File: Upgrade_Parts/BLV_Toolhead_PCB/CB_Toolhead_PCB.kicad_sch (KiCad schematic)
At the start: 10 parts, among them J1 Micro-Fit, J2 JST-4, J3 JST-2, J4 JST-2, J5 JST-2, J6 JST-2, J7 Endstop, J8 JST-3, J9 JST-2

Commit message: termination fix
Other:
- note added: "Accelerometer LIS3DH RJ45 Con"
- note removed: "Accelerometer"
- company: (none) -> https://github.com/Battosai42/CraftbotPlus_Upgrade
- title: (none) -> BLF Toolhaed PCB
- moved on the sheet: J1, J2, TH1

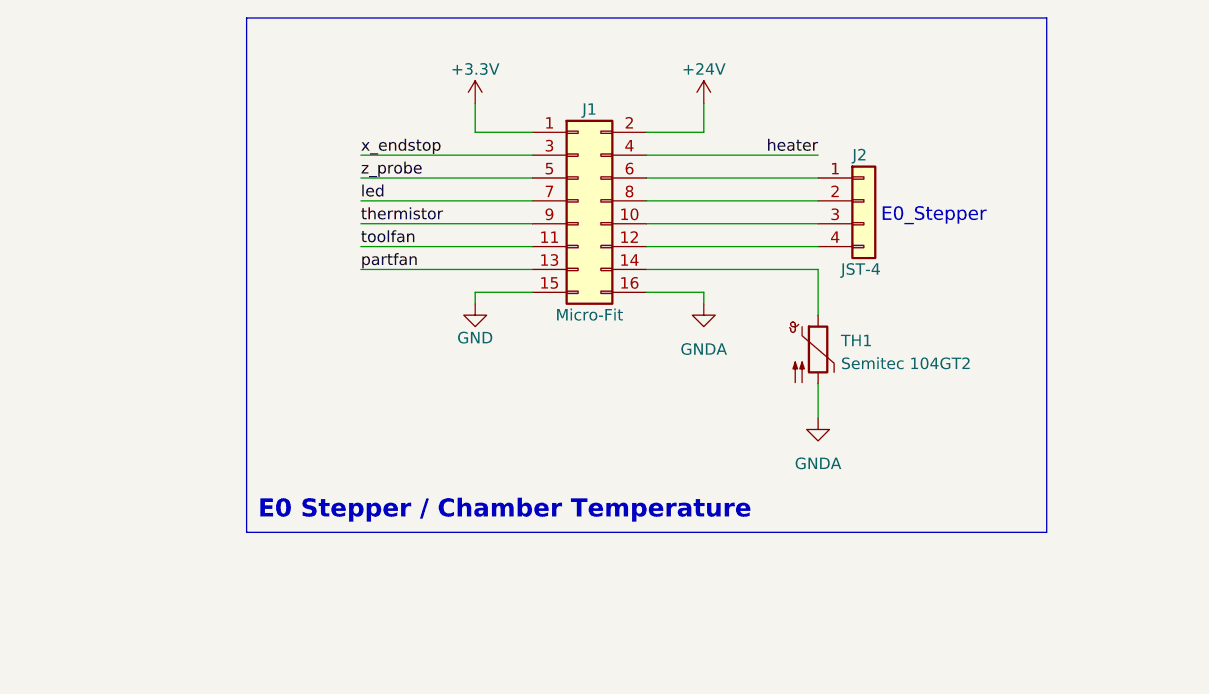
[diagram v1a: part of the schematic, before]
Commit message: using 3.3V LVDS driver
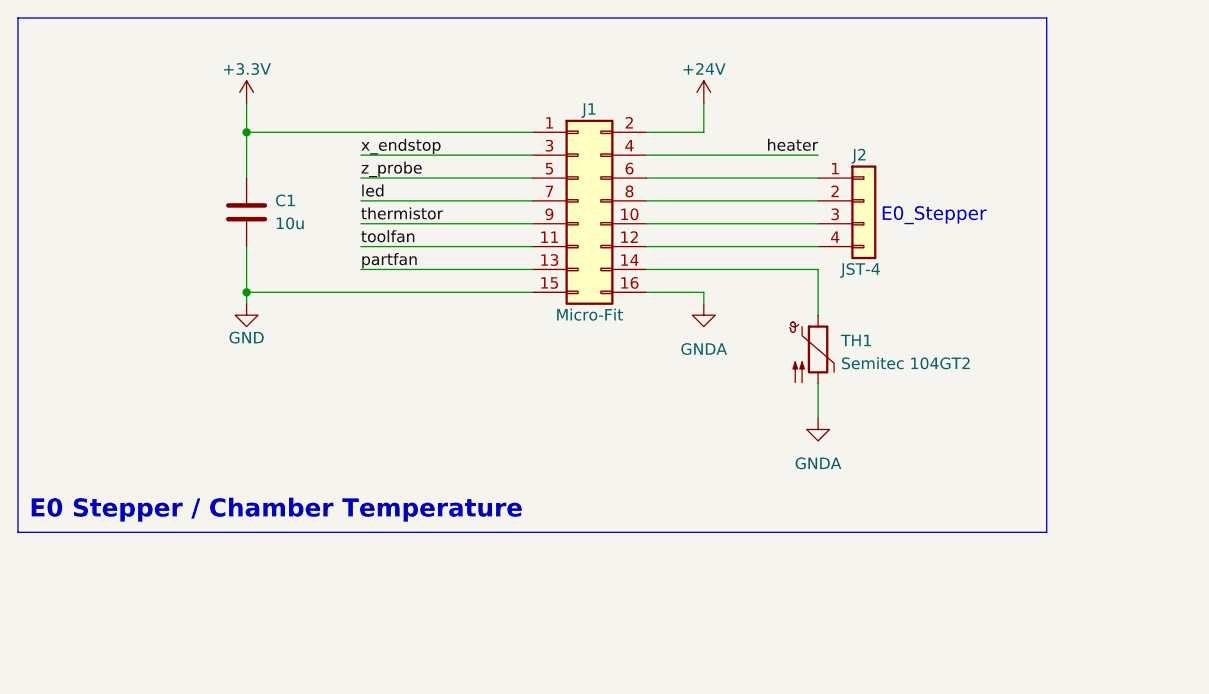
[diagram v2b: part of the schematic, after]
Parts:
- added C1: 10u, symbol Device:C
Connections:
- net +3V3: now also C1.1
- net GND: now also C1.2

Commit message: cleanup
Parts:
- added H1, H2, H3, H4: M3_Mount, symbol Mechanical:MountingHole_Pad
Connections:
- net GND: now also H1.1, H2.1, H3.1, H4.1
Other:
- note added: "Accelerometer"
- note added: "LIS3DH RJ45 Con"
- note removed: "Accelerometer LIS3DH RJ45 Con"
- moved on the sheet: C1, J1, J2, TH1

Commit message: replaced lvds drver
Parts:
- C1: footprint (none) -> Capacitor_SMD:C_0603_1608Metric
- H1, H2, H3, H4: footprint (none) -> MountingHole:MountingHole_3.2mm_M3_DIN965_Pad
- J1: footprint Connector_Molex:Molex_Micro-Fit_3.0_43045-1612_2x08_P3.00mm_Vertical -> Connector_Molex:Molex_Micro-Fit_3.0_43045-1621_2x08-1MP_P3.00mm_Horizontal
- J7: footprint (none) -> Connector_JST:JST_EH_B3B-EH-A_1x03_P2.50mm_Vertical

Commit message: new page for periphery
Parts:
- removed J3, J4, J5, J6, J9: JST-2, Connector_JST:JST_EH_B2B-EH-A_1x02_P2.50mm_Vertical, symbol Connector_Generic:Conn_01x02
- removed J7: Endstop, Connector_JST:JST_EH_B3B-EH-A_1x03_P2.50mm_Vertical, symbol Connector_Generic:Conn_01x03
- removed J8: JST-3, Connector_JST:JST_EH_B3B-EH-A_1x03_P2.50mm_Vertical, symbol Connector_Generic:Conn_01x03
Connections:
- net 1A: now reaches J1.6 (Pin_6), J2.1 (Pin_1)
- net 1B: now reaches J1.8 (Pin_8), J2.2 (Pin_2)
- net 2A: now reaches J1.10 (Pin_10), J2.3 (Pin_3)
- net 2B: now reaches J1.12 (Pin_12), J2.4 (Pin_4)
- no-connect marks 1 -> 0
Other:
- added sheet Periphery (periphery.kicad_sch)
- note added: "Board2Wire Connector"
- note added: "Extruder"
- note removed: "E0 Stepper / Chamber Temperature"
- note removed: "E0_Heater"
- note removed: "E0_Partfan"
- note removed: "E0_Thermistor"
- note removed: "E0_Toolfan"
- note removed: "Hotend / Endstop / Probe"
- note removed: "IR_Probe"
- note removed: "Toolhead LED"
- note removed: "X-Endstop"
- moved on the sheet: C1, J1, J2, TH1

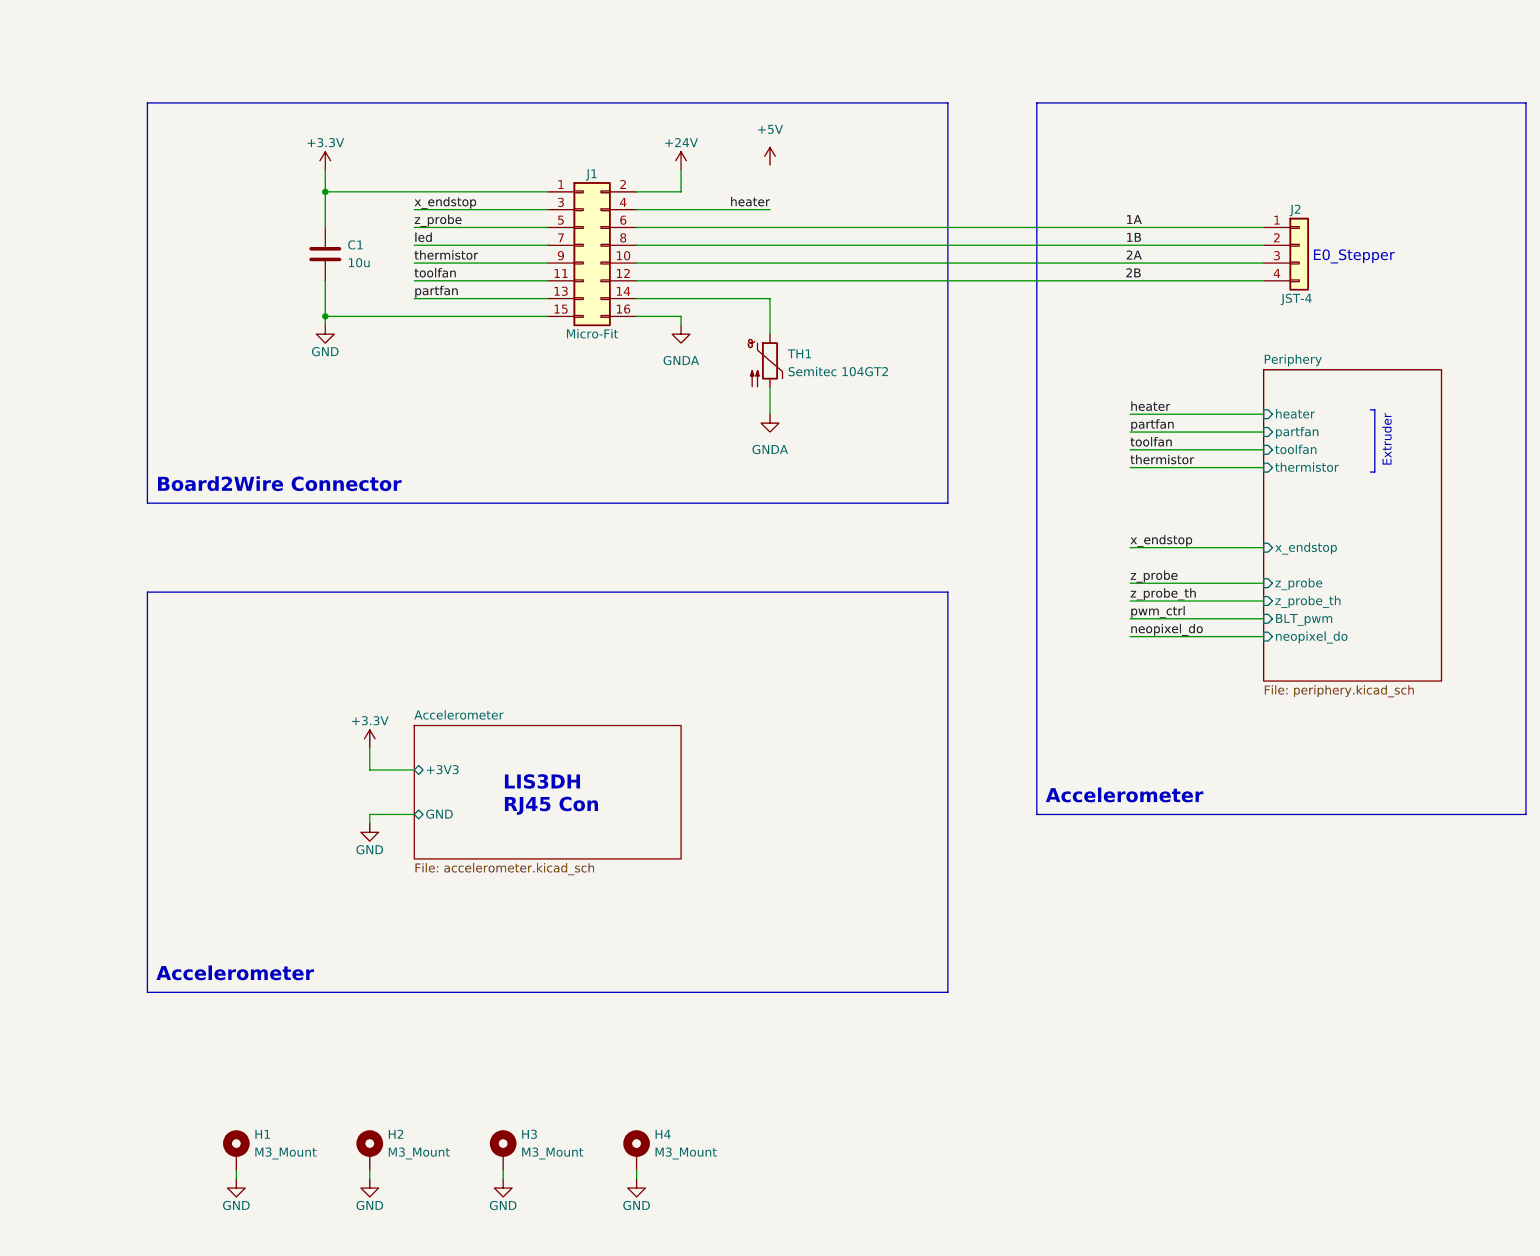
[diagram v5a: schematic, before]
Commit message: removed lvds drivers
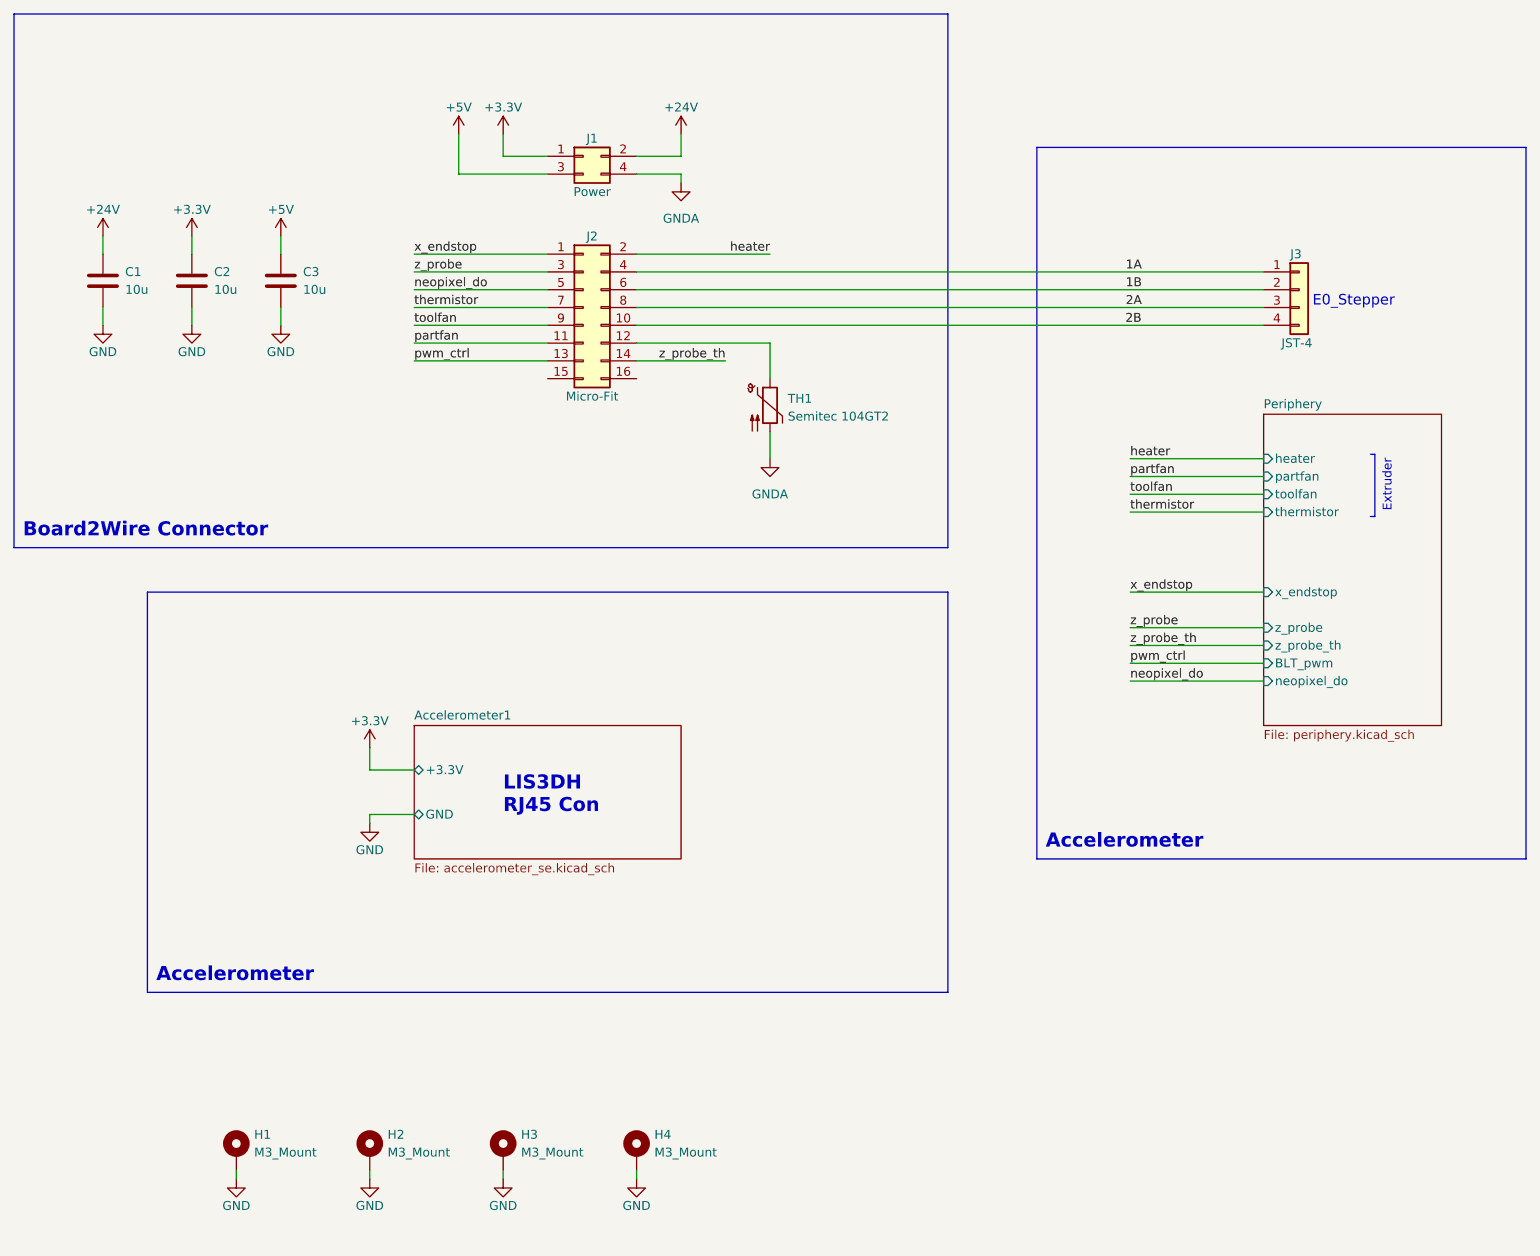
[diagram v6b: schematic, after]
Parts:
- added C1, C2: 10u, Capacitor_SMD:C_0603_1608Metric, symbol Device:C
- added J1: Power, Connector_Molex:Molex_Micro-Fit_3.0_43045-0421_2x02-1MP_P3.00mm_Horizontal, symbol Connector_Generic:Conn_02x02_Odd_Even
- renumbered C1 to C3, J1 to J2, J2 to J3
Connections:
- net led is gone; now on net thermistor: J2.7 (Pin_7)
- net +24V: now also C1.1, J1.2 (Pin_2); no longer J2.2 (Pin_2)
- net +3V3: now also C2.1, J1.1 (Pin_1); no longer C3.1, J2.1 (Pin_1)
- net +5V: now also C3.1, J1.3 (Pin_3)
- net 1A: now also J2.4 (Pin_4); no longer J2.6 (Pin_6)
- net 1B: now also J2.6 (Pin_6); no longer J2.8 (Pin_8)
- net 2A: now also J2.8 (Pin_8); no longer J2.10 (Pin_10)
- net 2B: now also J2.10 (Pin_10); no longer J2.12 (Pin_12)
- net GND: now also C1.2, C2.2; no longer J2.15 (Pin_15)
- net GNDA: now also J1.4 (Pin_4); no longer J2.16 (Pin_16)
- net heater: now also J2.2 (Pin_2); no longer J2.4 (Pin_4)
- net neopixel_do: now also J2.5 (Pin_5)
- net partfan: now also J2.11 (Pin_11); no longer J2.13 (Pin_13)
- net pwm_ctrl: now also J2.13 (Pin_13)
- net thermistor: no longer J2.9 (Pin_9)
- net toolfan: now also J2.9 (Pin_9); no longer J2.11 (Pin_11)
- net x_endstop: now also J2.1 (Pin_1); no longer J2.3 (Pin_3)
- net z_probe: now also J2.3 (Pin_3); no longer J2.5 (Pin_5)
- net z_probe_th: now also J2.14 (Pin_14)
- net at TH1.1: now also J2.12 (Pin_12); no longer J2.14 (Pin_14)
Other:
- removed sheet Accelerometer
- added sheet Accelerometer1 (accelerometer_se.kicad_sch)
- moved on the sheet: C3, J2, J3, TH1
